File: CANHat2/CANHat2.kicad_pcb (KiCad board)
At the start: 2 copper layers, 65 x 56 mm, 27 parts, among them J0 RPi_GPIO, J1 SPI Select, J2 PWR Select, J3 RJ45, J4 RJ45, J5 Termination, T1 12 Volts, U1 MCP2515, U2 ISO1050DUB, U3 LM78L05ACZ, X1 8 MHz

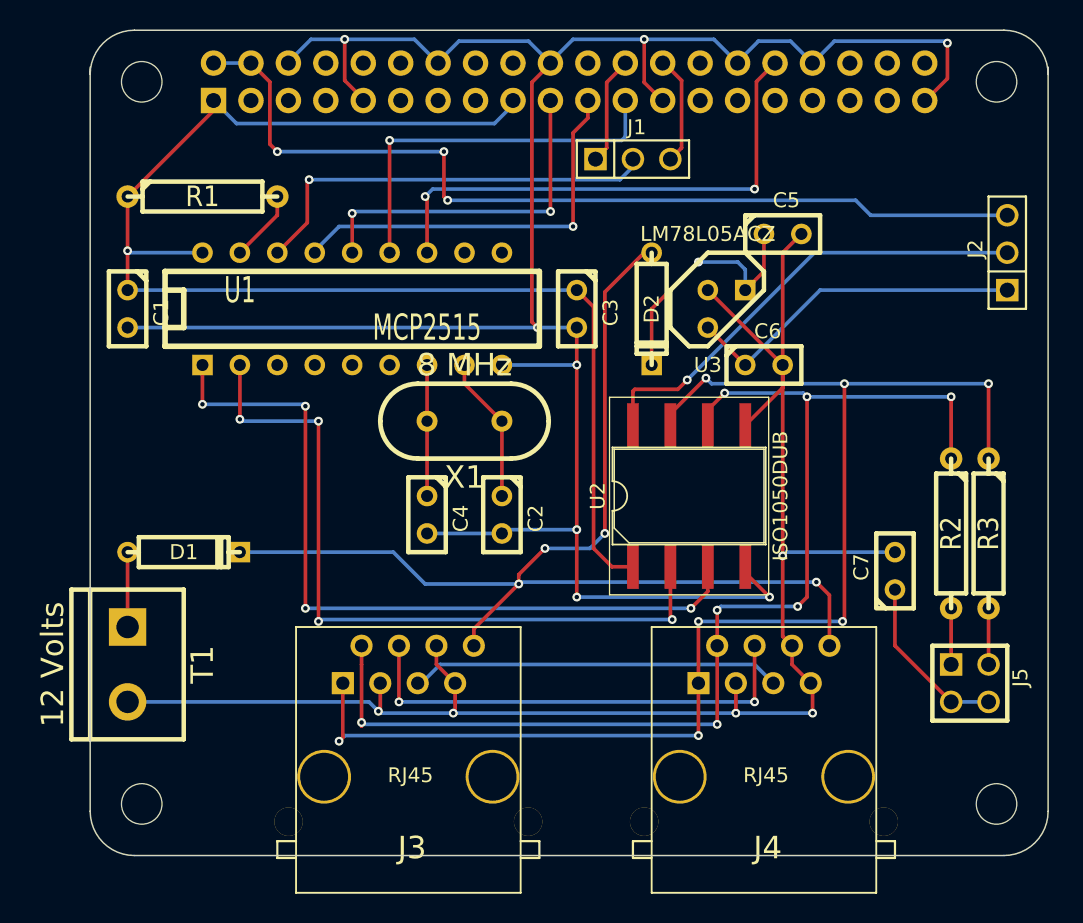
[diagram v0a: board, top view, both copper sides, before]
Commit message: Update module for C1. Adjust silk screen labels.
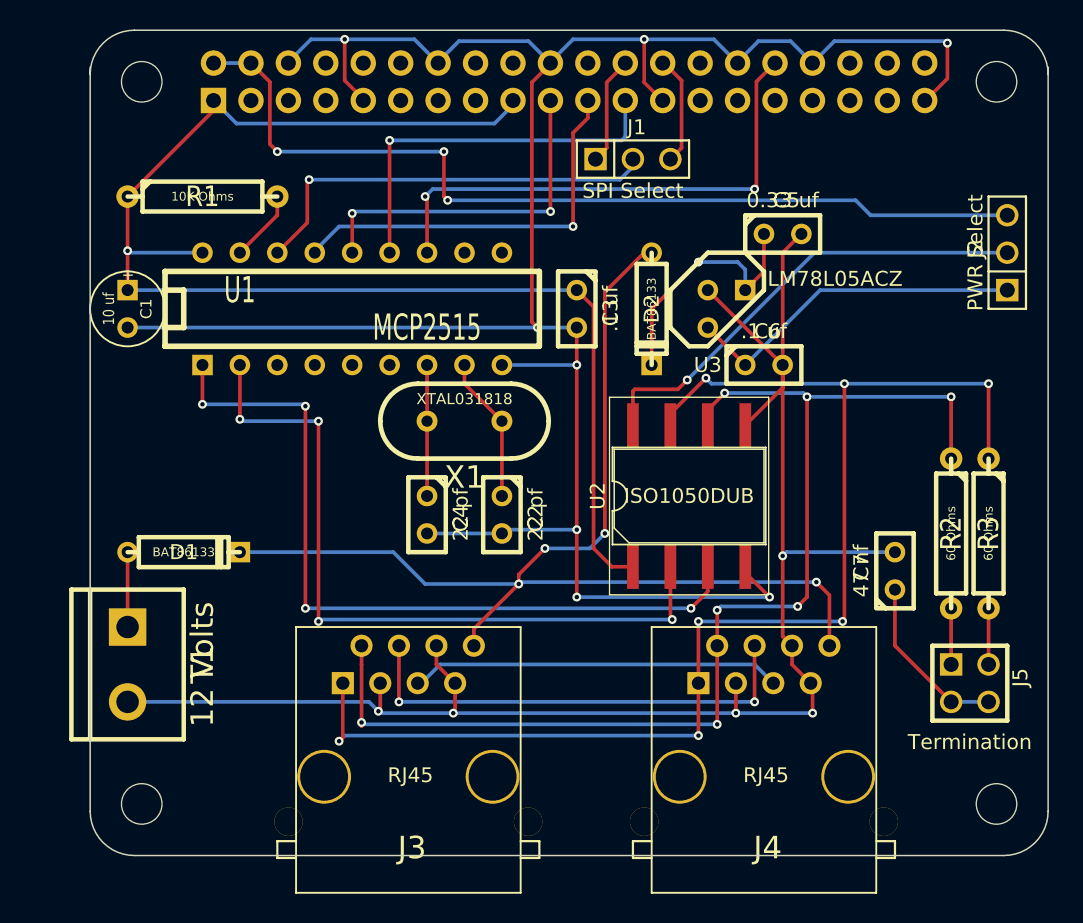
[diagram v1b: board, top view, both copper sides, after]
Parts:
- C1: footprint C1 -> C1V5
- D1, D2: value DIODESCH -> BAT86133
- X1: value 8 MHz -> XTAL031818

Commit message: Add copyright notice to CANHat2.
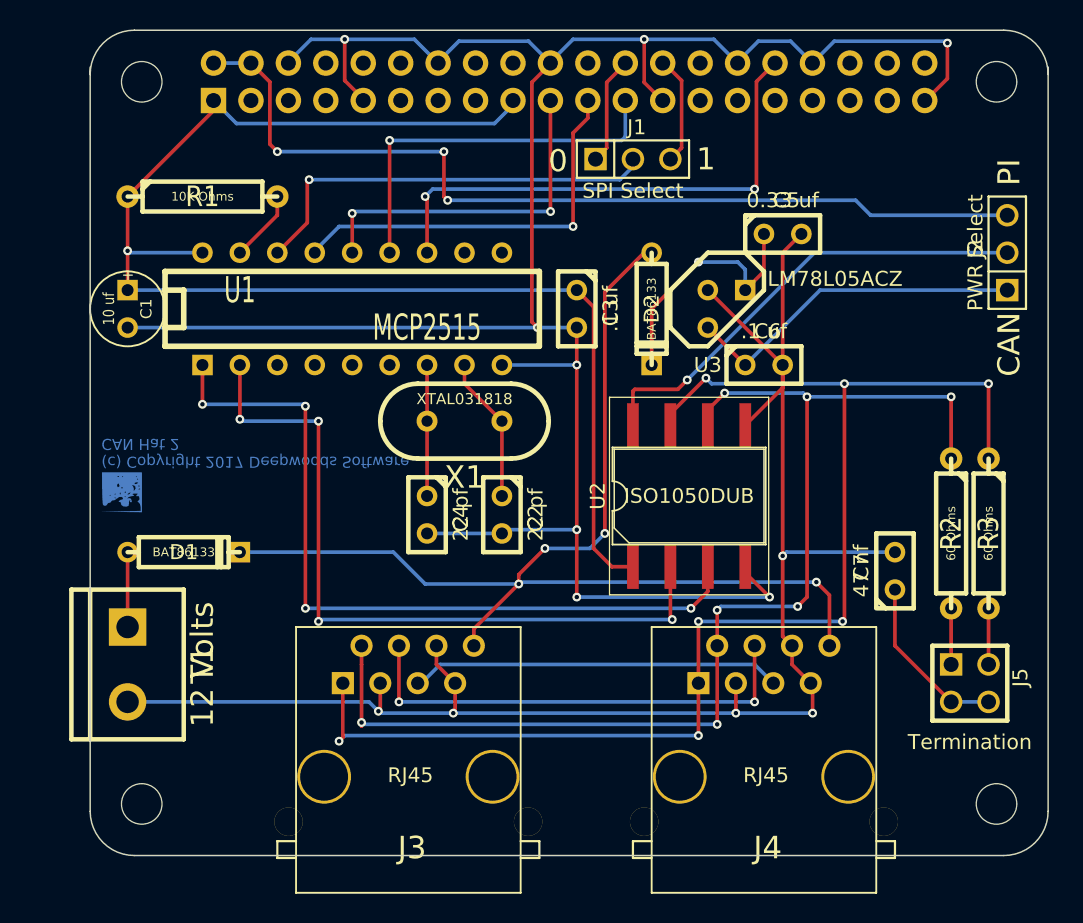
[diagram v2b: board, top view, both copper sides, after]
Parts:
- added ?: , DWSLogoBCU, F.Cu at (40.3, 63.2)
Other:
- board text added: "(c) Copyright 2017 Deepwoods Software CAN Hat 2"
- board text added: "0"
- board text added: "1"
- board text added: "CAN"
- board text added: "PI"
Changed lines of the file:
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@@
     (links 67)
     (no_connects 0)
-    (area 29.28939 20.694 130.847429 101.769)
+    (area 15.751288 20.694 130.847429 101.769)
     (thickness 1.6)
-    (drawings 16)
+    (drawings 21)
     (tracks 287)
     (zones 0)
-    (modules 27)
+    (modules 28)
     (nets 29)
   )
@@
     )
   )
+  (module DWSLogoBCU (layer F.Cu)
+    (at 40.259 63.246 180)
+    (fp_text reference "" (at 0 0 180) (layer F.SilkS)
+      (effects (font (size 1.524 1.524) (thickness 0.15)))
+    )
+    (fp_text value "" (at 0 0 180) (layer F.SilkS)
+      (effects (font (size 1.524 1.524) (thickness 0.15)))
+    )
+    (fp_poly (pts (xy 1.397 -1.31826) (xy 0.0635 -1.29286) (xy -1.27 -1.26492) (xy -1.27 -1.01854)
+      (xy -1.2192 -0.79502) (xy -1.12268 -0.6858) (xy -1.04648 -0.61722) (xy -1.0795 -0.5969)
+      (xy -1.16586 -0.52324) (xy -1.18618 -0.42418) (xy -1.15824 -0.28956) (xy -1.12268 -0.26416)
+      (xy -0.9779 -0.26416) (xy -0.97028 -0.20828) (xy -1.016 -0.17018) (xy -1.06934 -0.11176)
+      (xy -0.9779 -0.0889) (xy -0.889 -0.0889) (xy -0.72898 -0.09906) (xy -0.7239 -0.1397)
+      (xy -0.762 -0.17018) (xy -0.83312 -0.23368) (xy -0.75184 -0.254) (xy -0.71882 -0.254)
+      (xy -0.51054 -0.30226) (xy -0.42418 -0.34798) (xy -0.34544 -0.41402) (xy -0.41148 -0.40386)
+      (xy -0.43688 -0.3937) (xy -0.58166 -0.41656) (xy -0.62738 -0.47752) (xy -0.6731 -0.62738)
+      (xy -0.635 -0.67564) (xy -0.58928 -0.67818) (xy -0.54102 -0.62484) (xy -0.5588 -0.57912)
+      (xy -0.56896 -0.5207) (xy -0.52832 -0.53848) (xy -0.47244 -0.65532) (xy -0.48006 -0.75184)
+      (xy -0.4572 -0.90424) (xy -0.30988 -0.9779) (xy -0.09144 -0.95758) (xy 0.04572 -0.86614)
+      (xy 0.0635 -0.77216) (xy 0.09652 -0.66802) (xy 0.15494 -0.65786) (xy 0.22352 -0.63246)
+      (xy 0.21336 -0.59436) (xy 0.0889 -0.51562) (xy 0.0381 -0.508) (xy -0.07366 -0.46482)
+      (xy -0.05588 -0.37338) (xy 0.04318 -0.30734) (xy 0.19304 -0.32512) (xy 0.3429 -0.42926)
+      (xy 0.49276 -0.53594) (xy 0.5969 -0.54864) (xy 0.69088 -0.56896) (xy 0.72898 -0.62992)
+      (xy 0.80772 -0.71882) (xy 0.85598 -0.71374) (xy 0.94488 -0.7366) (xy 0.98298 -0.8001)
+      (xy 1.08966 -0.91694) (xy 1.22428 -0.90678) (xy 1.2954 -0.81788) (xy 1.31318 -0.69088)
+      (xy 1.32842 -0.43434) (xy 1.34112 -0.08382) (xy 1.34874 0.32512) (xy 1.35636 1.35382)
+      (xy 0.84582 1.35382) (xy 0.84582 -0.21082) (xy 0.80518 -0.254) (xy 0.762 -0.21082)
+      (xy 0.80518 -0.17018) (xy 0.84582 -0.21082) (xy 0.84582 1.35382) (xy 0.508 1.35382)
+      (xy 0.508 -0.127) (xy 0.508 -0.381) (xy 0.46482 -0.42418) (xy 0.42418 -0.381)
+      (xy 0.46482 -0.33782) (xy 0.508 -0.381) (xy 0.508 -0.127) (xy 0.46482 -0.17018)
+      (xy 0.42418 -0.127) (xy 0.46482 -0.08382) (xy 0.508 -0.127) (xy 0.508 1.35382)
+      (xy 0.33782 1.35382) (xy 0.33782 0.46482) (xy 0.2921 0.35306) (xy 0.254 0.33782)
+      (xy 0.1778 0.4064) (xy 0.17018 0.46482) (xy 0.21336 0.57912) (xy 0.254 0.59182)
+      (xy 0.32766 0.52324) (xy 0.33782 0.46482) (xy 0.33782 1.35382) (xy 0.32258 1.35382)
+      (xy 0.32258 1.06934) (xy 0.30988 1.04394) (xy 0.20828 1.03378) (xy 0.19812 1.04394)
+      (xy 0.20828 1.09474) (xy 0.254 1.09982) (xy 0.32258 1.06934) (xy 0.32258 1.35382)
+      (xy 0.14986 1.35382) (xy 0.14986 -0.12954) (xy 0.1397 -0.14224) (xy 0.09144 -0.12954)
+      (xy 0.08382 -0.08382) (xy 0.1143 -0.01524) (xy 0.1397 -0.02794) (xy 0.14986 -0.12954)
+      (xy 0.14986 1.35382) (xy 0.06858 1.35382) (xy 0.06858 0.30734) (xy 0.05588 0.28194)
+      (xy -0.04572 0.27178) (xy -0.05588 0.28194) (xy -0.04572 0.33274) (xy 0 0.33782)
+      (xy 0.06858 0.30734) (xy 0.06858 1.35382) (xy 0 1.35382) (xy 0 1.05918)
+      (xy -0.04318 1.016) (xy -0.08382 1.05918) (xy -0.04318 1.09982) (xy 0 1.05918)
+      (xy 0 1.35382) (xy -0.17018 1.35382) (xy -0.17018 -0.29718) (xy -0.21082 -0.33782)
+      (xy -0.254 -0.29718) (xy -0.21082 -0.254) (xy -0.17018 -0.29718) (xy -0.17018 1.35382)
+      (xy -0.18796 1.35382) (xy -0.18796 -0.04572) (xy -0.19812 -0.05588) (xy -0.24892 -0.04572)
+      (xy -0.254 0) (xy -0.22352 0.06858) (xy -0.19812 0.05588) (xy -0.18796 -0.04572)
+      (xy -0.18796 1.35382) (xy -0.37846 1.35382) (xy -0.37846 -0.1524) (xy -0.4699 -0.14478)
+      (xy -0.53086 -0.09652) (xy -0.5842 -0.0254) (xy -0.50038 -0.04318) (xy -0.4826 -0.04826)
+      (xy -0.381 -0.1143) (xy -0.37846 -0.1524) (xy -0.37846 1.35382) (xy -0.6985 1.35382)
+      (xy -0.6985 0.4953) (xy -0.70612 0.44958) (xy -0.75946 0.38354) (xy -0.81534 0.23368)
+      (xy -0.8001 0.16002) (xy -0.78486 0.09652) (xy -0.83312 0.11938) (xy -0.92456 0.24638)
+      (xy -0.89916 0.39116) (xy -0.8255 0.45212) (xy -0.6985 0.4953) (xy -0.6985 1.35382)
+      (xy -0.84582 1.35382) (xy -0.84582 0.59436) (xy -0.90932 0.54864) (xy -0.97282 0.56134)
+      (xy -1.08458 0.6223) (xy -1.09982 0.64262) (xy -1.03124 0.6731) (xy -0.97282 0.67818)
+      (xy -0.86106 0.63246) (xy -0.84582 0.59436) (xy -0.84582 1.35382) (xy -0.93218 1.35382)
+      (xy -0.93218 1.05918) (xy -0.97282 1.016) (xy -1.016 1.05918) (xy -1.016 0.889)
+      (xy -1.05918 0.84582) (xy -1.09982 0.889) (xy -1.05918 0.93218) (xy -1.016 0.889)
+      (xy -1.016 1.05918) (xy -0.97282 1.09982) (xy -0.93218 1.05918) (xy -0.93218 1.35382)
+      (xy -1.11506 1.35382) (xy -1.11506 0.22352) (xy -1.1303 0.19812) (xy -1.22936 0.18796)
+      (xy -1.24206 0.19812) (xy -1.22936 0.24638) (xy -1.18618 0.254) (xy -1.11506 0.22352)
+      (xy -1.11506 1.35382) (xy -1.12014 1.35382) (xy -1.12014 0.37846) (xy -1.1303 0.36576)
+      (xy -1.17856 0.37846) (xy -1.18618 0.42418) (xy -1.1557 0.49276) (xy -1.1303 0.48006)
+      (xy -1.12014 0.37846) (xy -1.12014 1.35382) (xy -1.35382 1.35382) (xy -1.35382 0)
+      (xy -1.35382 -1.35382) (xy 0.02032 -1.33604) (xy 1.397 -1.31826) (xy 1.397 -1.31826)) (layer B.Cu) (width 0.00254))
+  )
+  (gr_text "(c) Copyright 2017 Deepwoods Software\nCAN Hat 2" (at 38.862 60.579 180) (layer B.Cu)
+    (effects (font (size 0.75 0.75) (thickness 0.15)) (justify left mirror))
+  )
+  (gr_text CAN (at 100.457 53.213 90) (layer F.SilkS)
+    (effects (font (size 1.5 1.5) (thickness 0.3)))
+  )
+  (gr_text PI (at 100.457 41.529 90) (layer F.SilkS)
+    (effects (font (size 1.5 1.5) (thickness 0.3)))
+  )
+  (gr_text 0 (at 69.85 40.767) (layer F.SilkS)
+    (effects (font (size 1.5 1.5) (thickness 0.3)))
+  )
+  (gr_text 1 (at 79.883 40.64) (layer F.SilkS)
+    (effects (font (size 1.5 1.5) (thickness 0.3)))
+  )
   (gr_arc (start 41.101 34.894) (end 38.101 34.894) (angle 90) (layer Edge.Cuts) (width 0.1))
